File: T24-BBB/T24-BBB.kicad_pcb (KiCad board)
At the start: 2 copper layers, 195.3 x 127.1 mm, 208 parts, among them J1 Port 1, J10 Port 10, J11 Port 11, J12 Port 12, J13 Port 13, J14 Port 14, J15 Port 15, J16 Port 16, J17 Port 17, J18 Port 18, J19 Port 19, J2 Port 2, J20 Port 20, J21 Port 21, J22 Port 22, J23 Port 23, J24 Port 24, J25 9-16 In, J26 1-8 In, J27 17-24 In, J28 5V In, J29 OLED, J3 Port 3, J30 5V Select, J31 VIN2_V, J32 VIN3_V, J33 VIN1_V, J34 25-28, J35 29-32, J36 33-36, J37 37-40, J38 41-44, J4 Port 4, J40 DMX2, J41 DMX1, J44 GPIO, J5 Port 5, J6 Port 6, J7 Port 7, J8 Port 8, J9 Port 9, SW2 Enter BTN, SW3 Down BTN, U1 74HC245D, U10 Buck, U11 BEAGLEBONEBLACK, U17 74HC245D, U2 AT24C256C, U3 AM26LS31CDR, U4 AM26LS31CDR, U5 AM26LS31CDR, U6 AM26LS31CDR, U7 AM26LS31CDR, U8 UA9638CD, U9 74HC245D

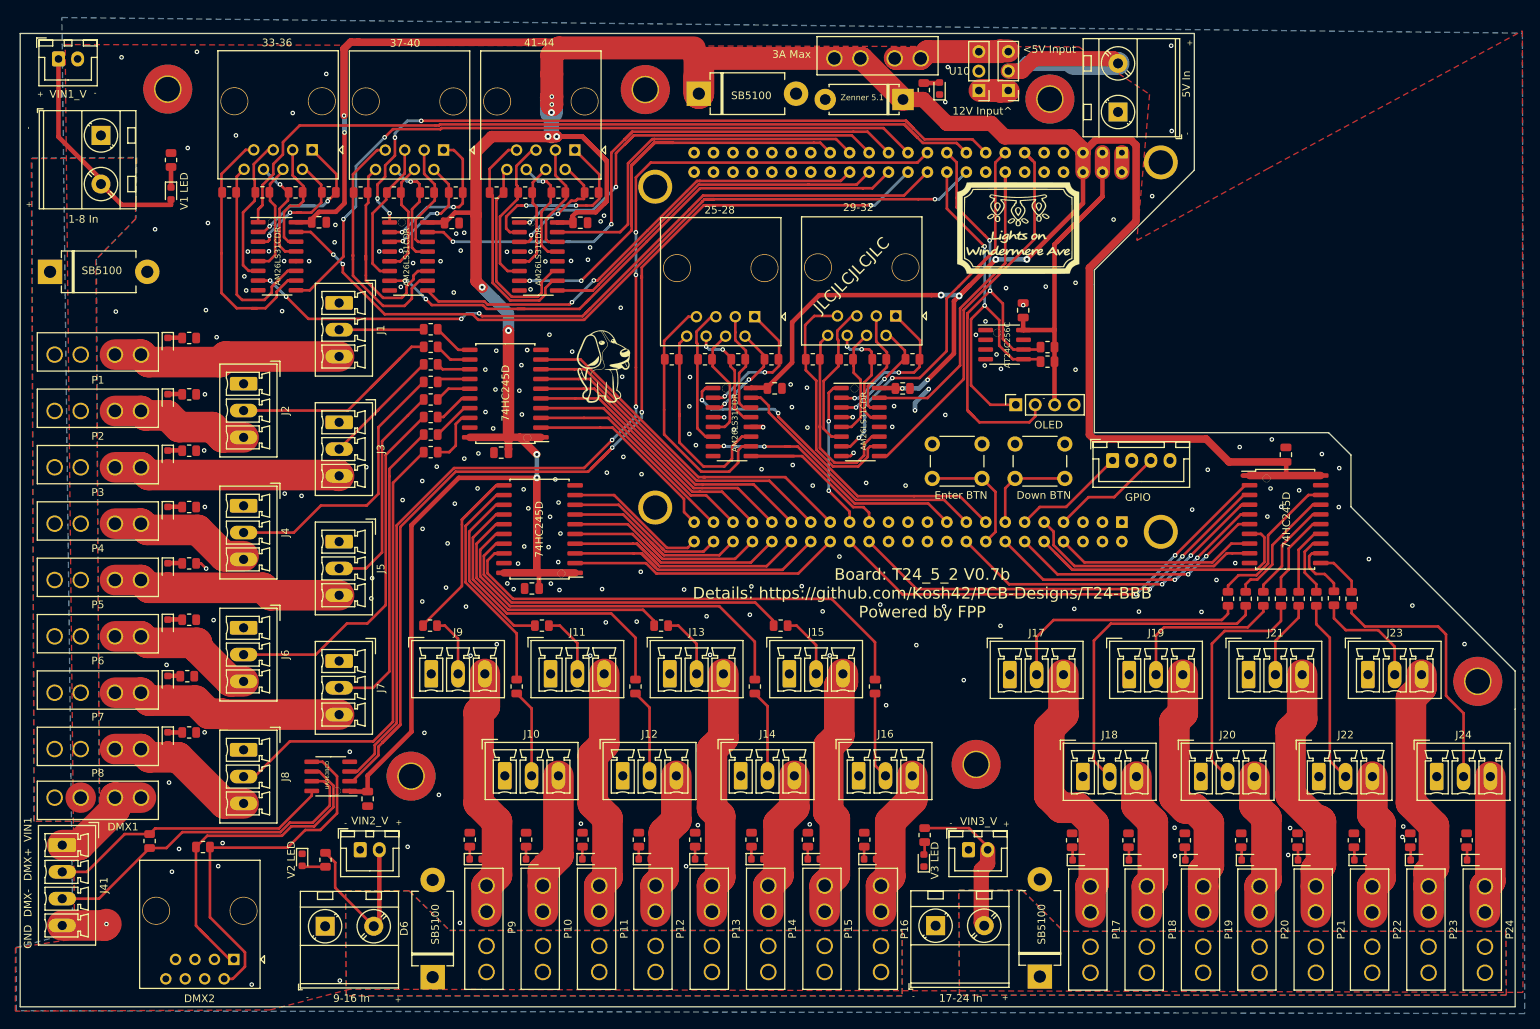
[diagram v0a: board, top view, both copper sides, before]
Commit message: 0.7
Buck and reroute
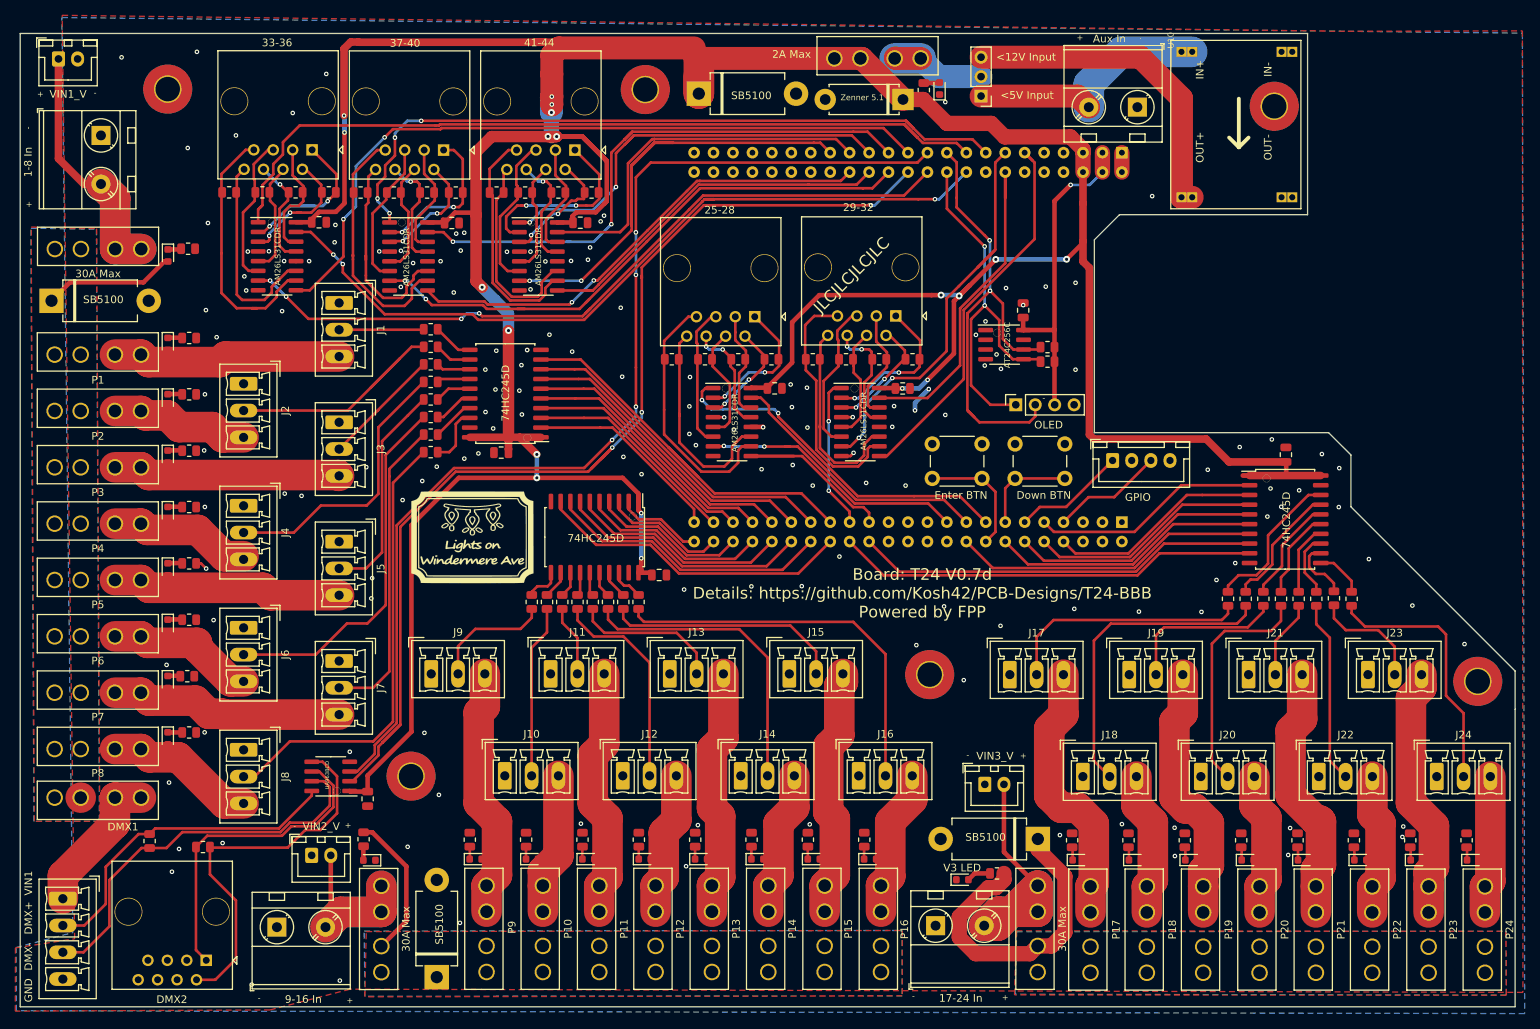
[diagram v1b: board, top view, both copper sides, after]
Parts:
- removed the G*** at (133.0, 71.3)
- added F25: 30A Max, 3544again:3544-2, F.Cu at (72.7, 56.0)
- added F26: 30A Max, 3544again:3544-2, F.Cu at (104.1, 139.2)
- added F27: 30A Max, 3544again:3544-2, F.Cu at (189.8, 139.2)
- F28: value 3A Max -> 2A Max
- J28: value 5V In -> Aux In
- U10: value Buck -> MP1584; footprint Connector_PinHeader_2.54mm:PinHeader_1x03_P2.54mm_Vertical -> MP1584:DC-BRICK
- moved G*** 81.9 mm to (116.0, 93.6)
- moved R9 32.8 mm to (137.7, 102.1)
- moved H1 29.3 mm to (220.7, 37.3)
- moved U10 25.9 mm to (207.2, 28.7), turned to 270 degrees
- moved R11 22.1 mm to (133.7, 102.1)
- moved R10 20.8 mm to (135.7, 102.1), turned to 90 degrees
- moved D7 18.0 mm to (189.9, 133.1), turned to 180 degrees
- moved C9 16.7 mm to (140.4, 98.6), turned to 0 degrees
- moved R16 13.6 mm to (123.8, 102.1), turned to 90 degrees
- moved R13 13.4 mm to (129.7, 102.1)
- moved H6 13.2 mm to (175.7, 111.6)
- moved R25 11.8 mm to (78.9, 56.0), turned to 0 degrees
- moved R15 11.7 mm to (125.7, 102.1)
- moved R27 10.7 mm to (184.5, 137.6), turned to 180 degrees
- moved R12 9.45 mm to (131.7, 102.1), turned to 90 degrees
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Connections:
- J25 pad 2: VIN2 -> V2
- J26 pad 2: VIN1 -> V1
- J27 pad 2: VIN3 -> V3
- J28 pad 2: V5_In -> Aux_In
- J30 pad 1: Buck -> Aux_In
- J30 pad 2: V5_In -> V5
- J30 pad 3: V5 -> Buck
- J31 pad 2: VIN2 -> V2
- J32 pad 2: VIN3 -> V3
- J33 pad 1: VIN1 -> V1
- J40 pad 3: (no net) -> Net-(J40-Pad3)
- J40 pad 4: (no net) -> Net-(J40-Pad4)
- J40 pad 5: (no net) -> Net-(J40-Pad5)
- J40 pad 6: (no net) -> Net-(J40-Pad6)
- U11 pad P8_10: DATA22 -> DATA19
- U11 pad P8_12: DATA21 -> DATA20
- U11 pad P8_14: DATA20 -> DATA21
- U11 pad P8_18: DATA19 -> DATA22
- U11 pad P8_20: (no net) -> Net-(U11-PadP8_20)
- U11 pad P8_21: (no net) -> Net-(U11-PadP8_21)
- U11 pad P8_22: (no net) -> Net-(U11-PadP8_22)
- U11 pad P8_23: (no net) -> Net-(U11-PadP8_23)
- U11 pad P8_24: (no net) -> Net-(U11-PadP8_24)
- U11 pad P8_25: (no net) -> Net-(U11-PadP8_25)
- U11 pad P8_26: (no net) -> Net-(U11-PadP8_26)
- U11 pad P8_28: DATA18 -> DATA23
- U11 pad P8_3: (no net) -> Net-(U11-PadP8_3)
- U11 pad P8_30: DATA17 -> DATA24
- U11 pad P8_32: DATA16 -> DATA9
- U11 pad P8_34: DATA15 -> DATA10
- U11 pad P8_36: DATA14 -> DATA11
- U11 pad P8_38: DATA13 -> DATA12
- U11 pad P8_4: (no net) -> Net-(U11-PadP8_4)
- U11 pad P8_40: DATA12 -> DATA13
- U11 pad P8_42: DATA11 -> DATA14
- U11 pad P8_44: DATA10 -> DATA15
- U11 pad P8_46: DATA9 -> DATA16
- U11 pad P8_5: (no net) -> Net-(U11-PadP8_5)
- U11 pad P8_6: (no net) -> Net-(U11-PadP8_6)
- U11 pad P8_8: DATA23 -> DATA18
- U11 pad P8_9: DATA24 -> DATA17
- U11 pad P9_10: (no net) -> Net-(U11-PadP9_10)
- U11 pad P9_12: (no net) -> Net-(U11-PadP9_12)
- U11 pad P9_16: (no net) -> Net-(U11-PadP9_16)
- U11 pad P9_32: (no net) -> Net-(U11-PadP9_32)
- U11 pad P9_33: (no net) -> Net-(U11-PadP9_33)
- U11 pad P9_34: (no net) -> Net-(U11-PadP9_34)
- U11 pad P9_35: (no net) -> Net-(U11-PadP9_35)
- U11 pad P9_36: (no net) -> Net-(U11-PadP9_36)
- U11 pad P9_37: (no net) -> Net-(U11-PadP9_37)
- U11 pad P9_38: (no net) -> Net-(U11-PadP9_38)
- U11 pad P9_39: (no net) -> Net-(U11-PadP9_39)
- U11 pad P9_40: (no net) -> Net-(U11-PadP9_40)
- U11 pad P9_41: (no net) -> Net-(U11-PadP9_41)
- U11 pad P9_42: (no net) -> Net-(U11-PadP9_42)
- U11 pad P9_7: (no net) -> Net-(U11-PadP9_7)
- U11 pad P9_8: (no net) -> Net-(U11-PadP9_8)
- U11 pad P9_9: (no net) -> Net-(U11-PadP9_9)
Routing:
- net Net-(R9-Pad2): track 64.2 -> 4.36 mm
- net V3: track 0.00 -> 55.6 mm
- net Net-(R11-Pad2): track 52.3 -> 3.37 mm
- net V1: track 0.00 -> 45.9 mm
- net Net-(R10-Pad2): track 46.7 -> 3.67 mm
- net Net-(J16-Pad2): track 11.3 -> 51.2 mm
- net +5V: track 581.6 -> 542.4 mm, vias 17 -> 19
- net Net-(R13-Pad2): track 40.5 -> 3.05 mm
- net V5_In: track 35.8 -> 0.00 mm
- net Buck: track 7.44 -> 42.7 mm
- net Aux_In: track 0.00 -> 32.9 mm
- net V2: track 0.00 -> 32.7 mm
- net Net-(R12-Pad2): track 35.2 -> 3.07 mm
- net DATA17: track 61.0 -> 30.5 mm, vias 2 -> 0
- net DATA18: track 57.4 -> 28.8 mm, vias 2 -> 0
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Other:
- outline, holes or cut-outs redrawn
- board text added: "<12V Input"
- board text added: "Board: T24 V0.7d Details: https://github.com/Kosh42/PCB-Designs/T24-BBB Powered by FPP"
- board text removed: "12V Input^"
- board text removed: "Board: T24_5_2 V0.7b Details: https://github.com/Kosh42/PCB-Designs/T24-BBB Powered by FPP"

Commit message: Updates. T24 to 7e
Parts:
- removed G***: LOGO, 3544again:logo1612
- J1, J10, J11, J12, J13, J14, J15, J16, J17, J18, J19, J2, J20, J21, J22, J23, J24, J3, J4, J5, J6, J7, J8, J9: footprint Connector_Phoenix_MC:PhoenixContact_MCV_1,5_3-G-3.5_1x03_P3.50mm_Vertical -> Logos:PhoenixContact_MCV_1,5_3-G-3.5_1x03_P3.50mm_Vertical_Tim
- moved J36 2.50 mm to (92.6, 43.1)
- moved R34 2.49 mm to (86.1, 48.6)
- moved R35 2.49 mm to (90.4, 48.6)
- moved R40 2.49 mm to (94.8, 48.6)
- moved R41 2.49 mm to (81.7, 48.6)
- moved J37 1.26 mm to (111.0, 43.1)
- moved R42 1.11 mm to (104.6, 48.6)
- moved R43 1.11 mm to (109.0, 48.6)
- moved R46 1.11 mm to (112.7, 48.6)
- moved R47 1.11 mm to (100.3, 48.6)
- moved C3 0.22 mm to (95.9, 52.7)
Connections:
- J33 pad 1: V1 -> GND
- J33 pad 2: GND -> V1
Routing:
- net Buck: track 42.7 -> 63.7 mm
- net Aux_In: track 32.9 -> 47.4 mm
- net GND: track 14.8 -> 21.2 mm, vias 152 -> 149
- net Net-(J36-Pad1): track 22.5 -> 17.8 mm
- net Net-(J36-Pad8): track 26.8 -> 31.3 mm
- net +5V: track 542.4 -> 546.6 mm, vias 19 -> 21
- net Net-(J37-Pad5): track 19.2 -> 22.8 mm
- net Net-(J36-Pad2): track 16.9 -> 13.9 mm
- net Net-(J37-Pad1): track 19.9 -> 17.2 mm
- net DATA33: track 106.5 -> 103.9 mm, vias 0 -> 2
- net V1: track 45.9 -> 43.5 mm
- net Net-(J36-Pad6): track 16.5 -> 14.3 mm
- net DATA36: track 96.2 -> 98.0 mm
- net Net-(J37-Pad4): track 15.0 -> 16.6 mm
- net DATA37: track 94.3 -> 92.8 mm
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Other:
- board text added: "Board: T24 V0.7e Details: https://github.com/Kosh42/PCB-Designs/T24-BBB Powered by FPP"
- board text removed: "Board: T24 V0.7d Details: https://github.com/Kosh42/PCB-Designs/T24-BBB Powered by FPP"
